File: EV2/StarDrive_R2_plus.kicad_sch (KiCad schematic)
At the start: 49 parts, among them J1 Conn_02x06_Odd_Even, J2 Conn_02x06_Odd_Even, J3 Conn_02x17_Odd_Even, J4 Conn_02x13_Odd_Even, J5 DBG1, U1 PCF8573P, U2 74HCT74, U3 74HCT04, U4 AM5380, U5 SN74F32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

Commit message: Fix #3 #4
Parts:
- C1: Part (none) -> JZ300
- RN4, RN5, RN6, RN7: footprint Resistor_SMD:R_Array_Convex_4x1206 -> Resistor_SMD:R_Array_Convex_4x0603
- Y1: footprint Crystal:Crystal_SMD_0603-2Pin_6.0x3.5mm -> Crystal:Crystal_SMD_3215-2Pin_3.2x1.5mm; Part (none) -> CC7V-T1A-32.768kHz-12.5pF-20PPM-TC-QC

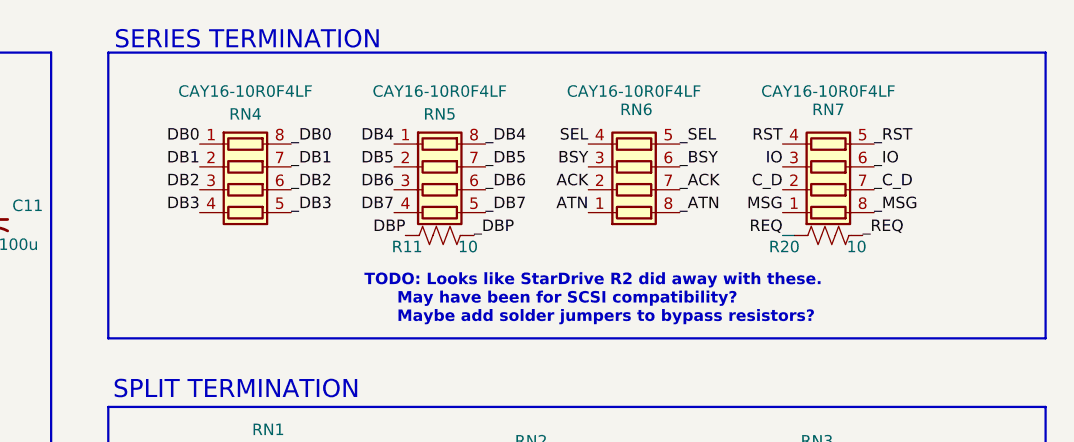
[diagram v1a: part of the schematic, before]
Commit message: Remove SMD resistor arrays with individual resistors and switch to hand-solder footprints.
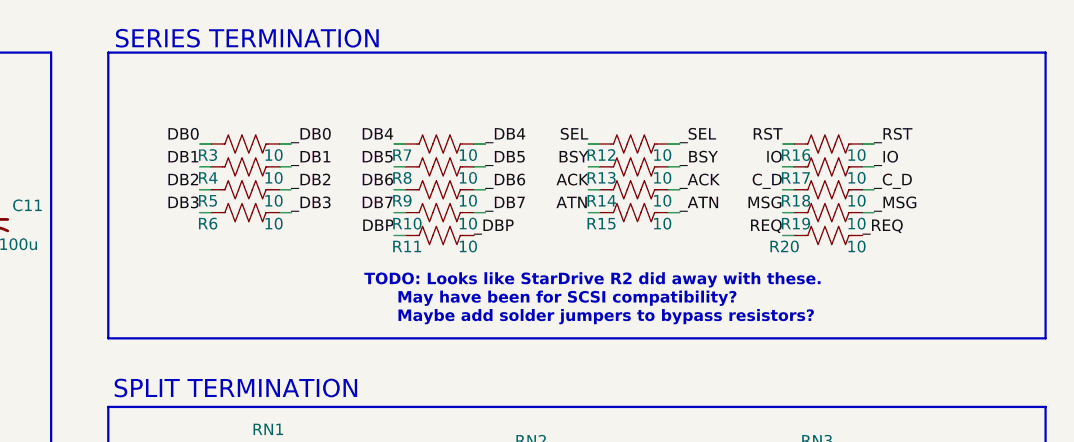
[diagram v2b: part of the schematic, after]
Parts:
- removed RN4, RN5, RN6, RN7: CAY16-10R0F4LF, Resistor_SMD:R_Array_Convex_4x0603, symbol Device:R_Pack04
- added R10, R12, R13, R14, R15, R16, R17, R18, R19, R3, R4, R5, R6, R7, R8, R9: 10, Resistor_SMD:R_0603_1608Metric_Pad0.98x0.95mm_HandSolder, symbol Device:R_US
- C2, C3, C4, C5, C6, C7, C8: footprint Capacitor_SMD:C_0603_1608Metric -> Capacitor_SMD:C_0603_1608Metric_Pad1.08x0.95mm_HandSolder
- D1, D5: footprint Diode_SMD:D_SOD-123 -> Diode_SMD:D_SOD-323_HandSoldering
- R1, R11, R2, R20, R21, R22, R23, R24: footprint Resistor_SMD:R_0603_1608Metric -> Resistor_SMD:R_0603_1608Metric_Pad0.98x0.95mm_HandSolder
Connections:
- net ACK: now also R14.1
- net ATN: now also R15.1
- net BSY: now also R13.1
- net C_D: now also R18.1
- net DB0: now also R3.1
- net DB1: now also R4.1
- net DB2: now also R5.1
- net DB3: now also R6.1
- net DB4: now also R7.1
- net DB5: now also R8.1
- net DB6: now also R9.1
- net DB7: now also R10.1
- net IO: now also R17.1
- net MSG: now also R19.1
- net RST: now also R16.1
- net SEL: now also R12.1
- net _ACK: now also R14.2
- net _ATN: now also R15.2
- net _BSY: now also R13.2
- net _C_D: now also R18.2
- net _DB0: now also R3.2
- net _DB1: now also R4.2
- net _DB2: now also R5.2
- net _DB3: now also R6.2
- net _DB4: now also R7.2
- net _DB5: now also R8.2
- net _DB6: now also R9.2
- net _DB7: now also R10.2
- net _IO: now also R17.2
- net _MSG: now also R19.2
- net _RST: now also R16.2
- net _SEL: now also R12.2
